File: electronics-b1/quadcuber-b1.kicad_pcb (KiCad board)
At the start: 2 copper layers, 99 x 99 mm, 70 parts, among them J1 9V DC 中心正, J10 舵机 R S+G, J11 EV3 R, J2 UART G TX RX, J20 舵机 L S+G, J21 EV3 L, J30 舵机 F S+G, J31 EV3 F, J40 舵机 B S+G, J41 EV3 B, Q1 IRF4905, U1 LM2596T-5.0, U10 DRV8871, U2 7805, U20 DRV8871, U3 Pico H, U30 DRV8871, U40 DRV8871

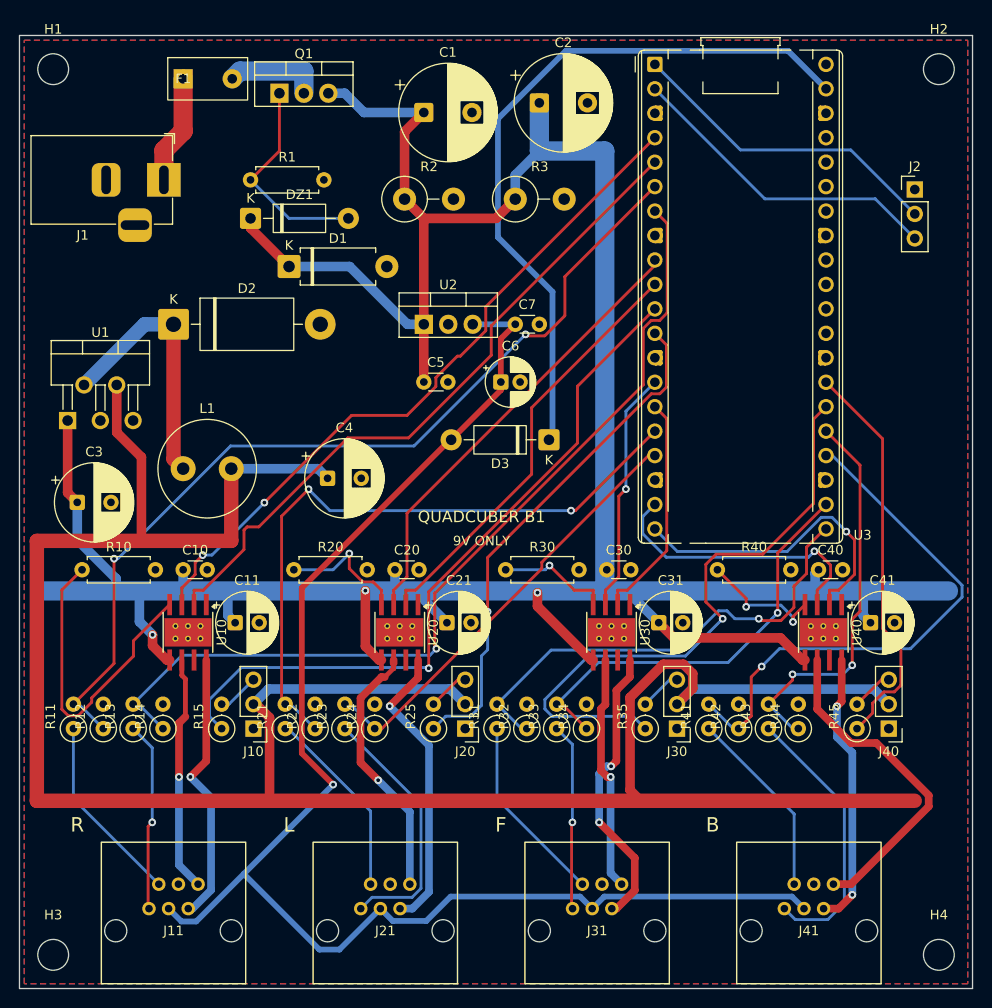
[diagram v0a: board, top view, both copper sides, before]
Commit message: B1 改为贴片为主：只保留插座和排针为通孔，并自带 3D 模型
- 用户要求元件尽量用贴片：P-MOS 改为 AO4407A（SOIC-8），舵机降压改为 LM2596S-5.0（TO-263-5），
  逻辑 5V 改为 AMS1117-5.0（SOT-223），二极管改为 SS34/SS14/SMBJ12A/BZT52C12，
  电阻电容改为 0805/2512，电解改为贴片铝电解，电感改为 12×12 贴片功率电感，保险丝改为 1206 慢断 8A。
  元件都放在顶面，便于热风枪手焊。
- 用户在 KiCad 3D 视图里看不到 Pico 和 DRV8871：KiCad Lite 不带标准 3D 库，DRV/EV3 的模型路径
  又指向 A1 工程。现把所用模型复制到 lib/3dmodels，统一用 ${KIPRJMOD} 引用。
- 布线：VM 主干改到底层 x=36 竖线 + y=57.4 横条（只覆盖四颗 DRV），两端留出底层通道；
  每个贴片接地脚就近打孔；铺铜后在至少一面是主地铜的位置打缝合过孔；KiCad 间距规则比
  freerouting 少 0.05mm 余量，消除 Pico 异形焊盘的近似误差。
- 结果：DRC 0 错误、0 未连通（26 条警告：丝印重叠和主干端点）；test_b1 5/5 通过；
  A1 及其首板包未改动。

Co-Authored-By: Claude Opus 5.5 <noreply@anthropic.com>
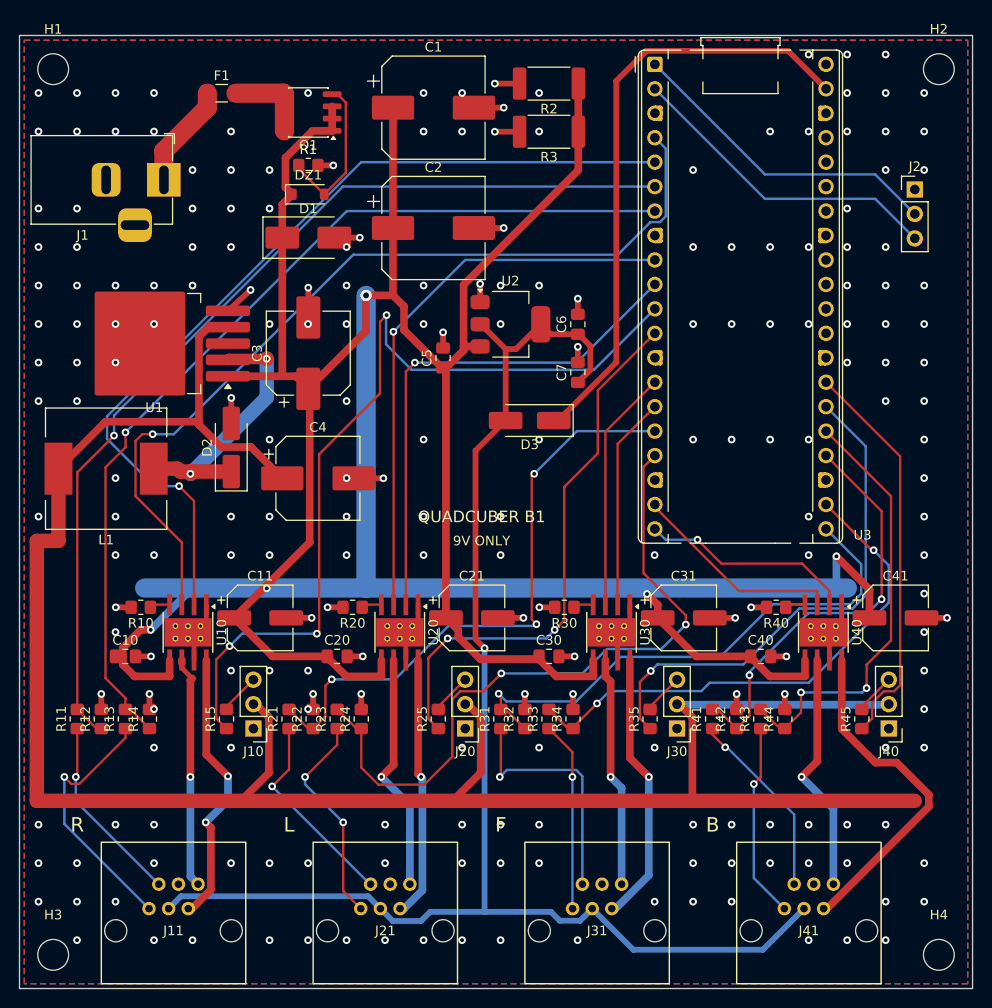
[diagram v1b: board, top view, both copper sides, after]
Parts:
- C1, C2: footprint B1:CP_Radial_D10.0mm_P5.00mm -> B1:CP_Elec_10x10.5
- C10, C20, C30, C40, C7: footprint B1:C_Disc_D3.0mm_W1.6mm_P2.50mm -> B1:C_0805_2012Metric_Pad1.18x1.45mm_HandSolder
- C11, C21, C31, C41: footprint B1:CP_Radial_D6.3mm_P2.50mm -> B1:CP_Elec_6.3x7.7
- C3, C4: footprint B1:CP_Radial_D8.0mm_P3.50mm -> B1:CP_Elec_8x10.5
- C5: value 0.33u -> 10u/25V; footprint B1:C_Disc_D3.0mm_W1.6mm_P2.50mm -> B1:C_0805_2012Metric_Pad1.18x1.45mm_HandSolder
- C6: value 10u/16V -> 22u/16V; footprint B1:CP_Radial_D5.0mm_P2.00mm -> B1:C_0805_2012Metric_Pad1.18x1.45mm_HandSolder
- D1: value P6KE15A -> SMBJ12A; footprint B1:D_DO-15_P10.16mm_Horizontal -> B1:D_SMB_Handsoldering
- D2: value 1N5822 -> SS34; footprint B1:D_DO-201AD_P15.24mm_Horizontal -> B1:D_SMA_Handsoldering
- D3: value 1N5819 -> SS14; footprint B1:D_DO-41_SOD81_P10.16mm_Horizontal -> B1:D_SMA_Handsoldering
- DZ1: footprint B1:D_DO-41_SOD81_P10.16mm_Horizontal -> B1:D_SOD-123
- F1: value PTC 5A -> 8A 慢断; footprint B1:Fuse_PTC_Radial_P5.10mm -> B1:Fuse_1206_3216Metric_Pad1.42x1.75mm_HandSolder
- L1: footprint B1:L_Radial_D10.0mm_P5.00mm_Fastron_07M -> B1:L_12x12mm_H8mm
- Q1: value IRF4905 -> AO4407A; footprint B1:TO-220-3_Vertical -> B1:SOIC-8_3.9x4.9mm_P1.27mm
- R1, R10, R20, R30, R40: footprint B1:R_Axial_DIN0207_L6.3mm_D2.5mm_P7.62mm_Horizontal -> B1:R_0805_2012Metric_Pad1.20x1.40mm_HandSolder
- R11, R12, R13, R14, R15, R21, R22, R23, R24, R25, R31, R32, R33, R34, R35, R41, R42, R43, R44, R45: footprint B1:R_Axial_DIN0207_L6.3mm_D2.5mm_P2.54mm_Vertical -> B1:R_0805_2012Metric_Pad1.20x1.40mm_HandSolder
- R2, R3: footprint B1:R_Axial_DIN0414_L11.9mm_D4.5mm_P5.08mm_Vertical -> B1:R_2512_6332Metric_Pad1.40x3.35mm_HandSolder
- U1: value LM2596T-5.0 -> LM2596S-5.0; footprint B1:TO-220-5_P3.4x3.7mm_StaggerOdd_Lead3.8mm_Vertical -> B1:TO-263-5_TabPin3
- U2: value 7805 -> AMS1117-5.0; footprint B1:TO-220-3_Vertical -> B1:SOT-223-3_TabPin2
- moved C3 28.6 mm to (80.0, 83.0), turned to 90 degrees
- moved R2 19.2 mm to (105.0, 55.0), turned to 180 degrees
- moved C2 17.0 mm to (93.0, 70.0)
- moved D2 14.1 mm to (72.0, 92.8), turned to 90 degrees
- moved U1 12.0 mm to (64.0, 82.0), turned to 180 degrees
- moved C10 10.8 mm to (61.0, 114.5)
- moved C20 10.8 mm to (83.0, 114.5)
- moved C30 10.8 mm to (105.0, 114.5)
- moved C40 10.8 mm to (127.0, 114.5)
- moved C6 10.0 mm to (108.0, 80.0), turned to 90 degrees
- moved U2 9.00 mm to (101.0, 80.0)
- moved C7 8.20 mm to (108.0, 85.0), turned to 90 degrees
- moved L1 8.00 mm to (59.0, 95.0), turned to 180 degrees
- moved R3 7.83 mm to (105.0, 60.0), turned to 180 degrees
- moved R10 7.24 mm to (62.6, 109.4), turned to 180 degrees
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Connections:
- Q1 pad 1: GATE -> VM
- Q1 pad 2: VIN_F -> VM
- U2 pad 1: VM -> GND
- U2 pad 2: GND -> 5V_LOGIC
- U2 pad 3: 5V_LOGIC -> VM
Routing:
- net GND: track 0.00 -> 84.1 mm, vias 0 -> 221
- net VM: track 319.9 -> 372.8 mm, vias 3 -> 5
- net R_ILIM: track 32.8 -> 2.11 mm
- net SERVO_5V: track 254.4 -> 225.1 mm
- net GP13: track 45.4 -> 72.1 mm, vias 0 -> 2
- net GP3: track 70.8 -> 92.7 mm, vias 0 -> 1
- net GP2: track 73.0 -> 92.4 mm, vias 2 -> 1
- net GP8: track 74.8 -> 90.0 mm, vias 1 -> 3
- net GP18: track 56.3 -> 43.9 mm, vias 1 -> 2
- net L_ILIM: track 13.8 -> 2.11 mm, vias 1 -> 0
- net GP6: track 47.0 -> 58.6 mm, vias 0 -> 1
- net VSYS: track 74.5 -> 62.9 mm
- net B_ILIM: track 13.3 -> 2.11 mm, vias 2 -> 0
- net GP20: track 65.0 -> 53.8 mm
- net GP15: track 32.5 -> 22.2 mm
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
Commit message: B1 补接口丝印并记录马达通道排查
首测时舵机插反、误插进 J2（UART），EV3 背面数针也出过错，原因是板上没有针序标识。
- 舵机排针逐针印 G/+/S，J2 印 GND/TX/RX 和 UART，EV3 背面第 1 针旁印 1
- 丝印数据放在 circuit.py（SILK/REF_MOVES），generate.py 生成时加上；
  label_interfaces.py 给已布线 PCB 补加，只改丝印、可重复运行
- R21/R31/R41 位号移到电阻下方，避免压住新标识；DRC 丝印重叠 23→16
- test_b1.py 新增：各标识与对应网络焊盘同行
- 重新导出 Gerber、预览、DRC（已生产的实物无这些丝印）
- docs/b1-motor-channel-debug.md：L 路 U20 第 8 脚、B 路 U40 第 3 脚虚焊，
  带电对比引脚与焊盘电压定位；修复后四路验收数据

Co-Authored-By: Claude Opus 5.5 <noreply@anthropic.com>
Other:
- board text added: "+"
- board text added: "1"
- board text added: "G"
- board text added: "GND"
- board text added: "RX"
- board text added: "S"
- board text added: "TX"
- board text added: "UART"
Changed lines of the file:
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@@
 		(tags "resistor handsolder")
 		(property "Reference" "R41"
-			(at 0 -1.65 90)
+			(at -3.3 0 0)
 			(layer "F.SilkS")
 			(effects
@@
 		(tags "resistor handsolder")
 		(property "Reference" "R21"
-			(at 0 -1.65 90)
+			(at -3.3 0 0)
 			(layer "F.SilkS")
 			(effects
@@
 		(tags "resistor handsolder")
 		(property "Reference" "R31"
-			(at 0 -1.65 90)
+			(at -3.3 0 0)
 			(layer "F.SilkS")
 			(effects
@@
 		(layer "Edge.Cuts")
 	)
+	(gr_text "GND"
+		(at 145.2 66 0)
+		(layer "F.SilkS")
+		(effects
+			(font
+				(size 1 1)
+				(thickness 0.15)
+			)
+			(justify left)
+		)
+	)
+	(gr_text "TX"
+		(at 145.2 68.539999 0)
+		(layer "F.SilkS")
+		(effects
+			(font
+				(size 1 1)
+				(thickness 0.15)
+			)
+			(justify left)
+		)
+	)
+	(gr_text "RX"
+		(at 145.2 71.08 0)
+		(layer "F.SilkS")
+		(effects
+			(font
+				(size 1 1)
+				(thickness 0.15)
+			)
+			(justify left)
+		)
+	)
+	(gr_text "S"
+		(at 76.5 116.92 0)
+		(layer "F.SilkS")
+		(effects
+			(font
+				(size 1 1)
+				(thickness 0.15)
+			)
+		)
+	)
+	(gr_text "+"
+		(at 76.5 119.46 0)
+		(layer "F.SilkS")
+		(effects
+			(font
+				(size 1 1)
+				(thickness 0.15)
+			)
+		)
+	)
+	(gr_text "G"
+		(at 76.5 122 0)
+		(layer "F.SilkS")
+		(effects
+			(font
+				(size 1 1)
+				(thickness 0.15)
+			)
+		)
+	)
 	(gr_text "9V ONLY"
 		(at 98 102.5 0)
@@
 		)
 	)
+	(gr_text "S"
+		(at 98.5 116.92 0)
+		(layer "F.SilkS")
+		(effects
+			(font
+				(size 1 1)
+				(thickness 0.15)
+			)
+		)
+	)
+	(gr_text "+"
+		(at 98.5 119.46 0)
+		(layer "F.SilkS")
+		(effects
+			(font
+				(size 1 1)
+				(thickness 0.15)
+			)
+		)
+	)
+	(gr_text "G"
+		(at 98.5 122 0)
+		(layer "F.SilkS")
+		(effects
+			(font
+				(size 1 1)
+				(thickness 0.15)
+			)
+		)
+	)
+	(gr_text "S"
+		(at 120.5 116.92 0)
+		(layer "F.SilkS")
+		(effects
+			(font
+				(size 1 1)
+				(thickness 0.15)
+			)
+		)
+	)
+	(gr_text "+"
+		(at 120.5 119.46 0)
+		(layer "F.SilkS")
+		(effects
+			(font
+				(size 1 1)
+				(thickness 0.15)
+			)
+		)
+	)
+	(gr_text "G"
+		(at 120.5 122 0)
+		(layer "F.SilkS")
+		(effects
+			(font
+				(size 1 1)
+				(thickness 0.15)
+			)
+		)
+	)
+	(gr_text "S"
+		(at 142.5 116.92 0)
+		(layer "F.SilkS")
+		(effects
+			(font
+				(size 1 1)
+				(thickness 0.15)
+			)
+		)
+	)
+	(gr_text "+"
+		(at 142.5 119.46 0)
+		(layer "F.SilkS")
+		(effects
+			(font
+				(size 1 1)
+				(thickness 0.15)
+			)
+		)
+	)
+	(gr_text "G"
+		(at 142.5 122 0)
+		(layer "F.SilkS")
+		(effects
+			(font
+				(size 1 1)
+				(thickness 0.15)
+			)
+		)
+	)
+	(gr_text "UART"
+		(at 143 74.2 0)
+		(layer "F.SilkS")
+		(effects
+			(font
+				(size 1 1)
+				(thickness 0.15)
+			)
+		)
+	)
 	(gr_text "QUADCUBER B1"
 		(at 98 100 0)
@@
 		)
 	)
+	(gr_text "1"
+		(at 70.15 138.16 0)
+		(layer "B.SilkS")
+		(effects
+			(font
+				(size 1 1)
+				(thickness 0.15)
+			)
+			(justify mirror)
+		)
+	)
+	(gr_text "1"
+		(at 92.15 138.16 0)
+		(layer "B.SilkS")
+		(effects
+			(font
+				(size 1 1)
+				(thickness 0.15)
+			)
+			(justify mirror)
+		)
+	)
+	(gr_text "1"
+		(at 114.15 138.16 0)
+		(layer "B.SilkS")
+		(effects
+			(font
+				(size 1 1)
+				(thickness 0.15)
+			)
+			(justify mirror)
+		)
+	)
+	(gr_text "1"
+		(at 136.15 138.16 0)
+		(layer "B.SilkS")
+		(effects
+			(font
+				(size 1 1)
+				(thickness 0.15)
+			)
+			(justify mirror)
+		)
+	)
